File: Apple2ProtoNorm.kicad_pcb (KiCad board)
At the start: 2 copper layers, 177.8 x 76.4 mm, 3 parts, among them J1 Apple II Bus Card Edge, J2 Apple II Bus Card Pin Header

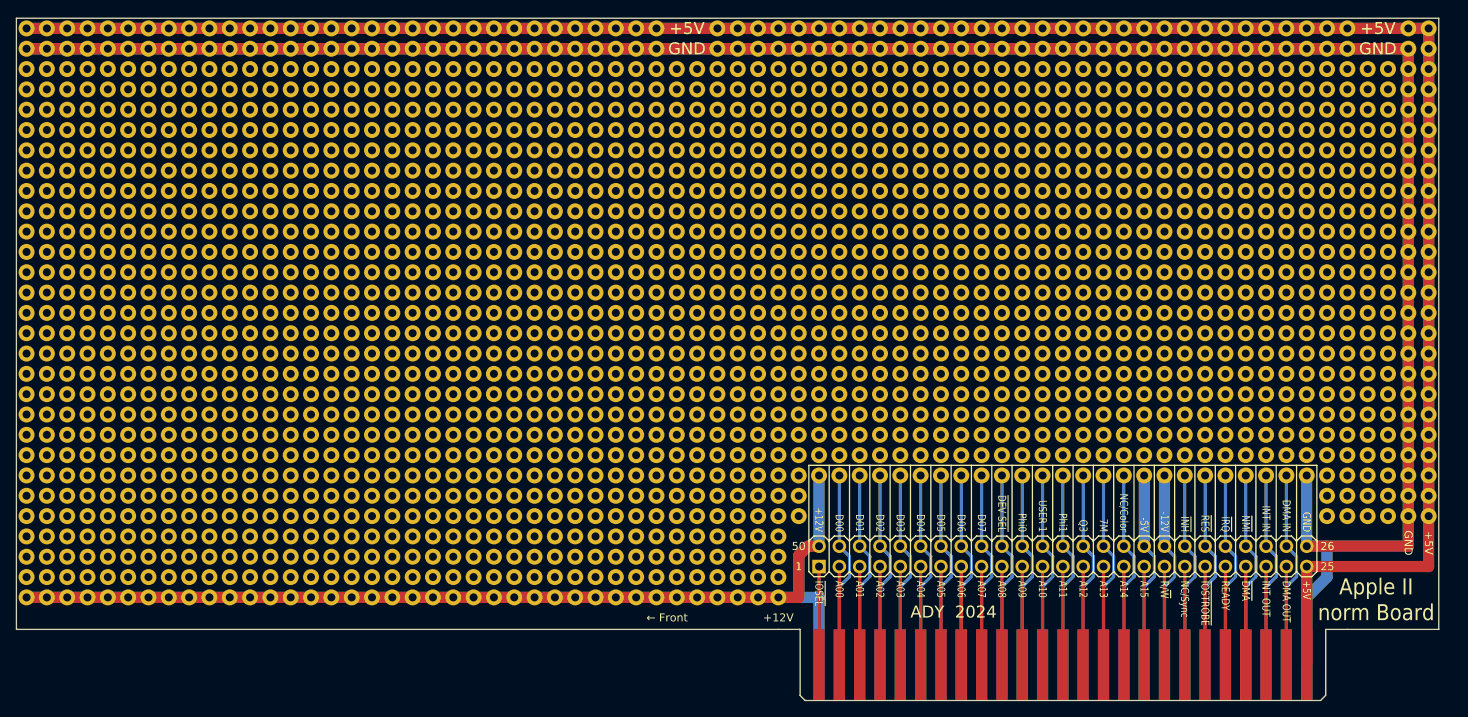
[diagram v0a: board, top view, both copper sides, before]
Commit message: Updated Silk Screen to be easier to read. Added more Apple II documentation.
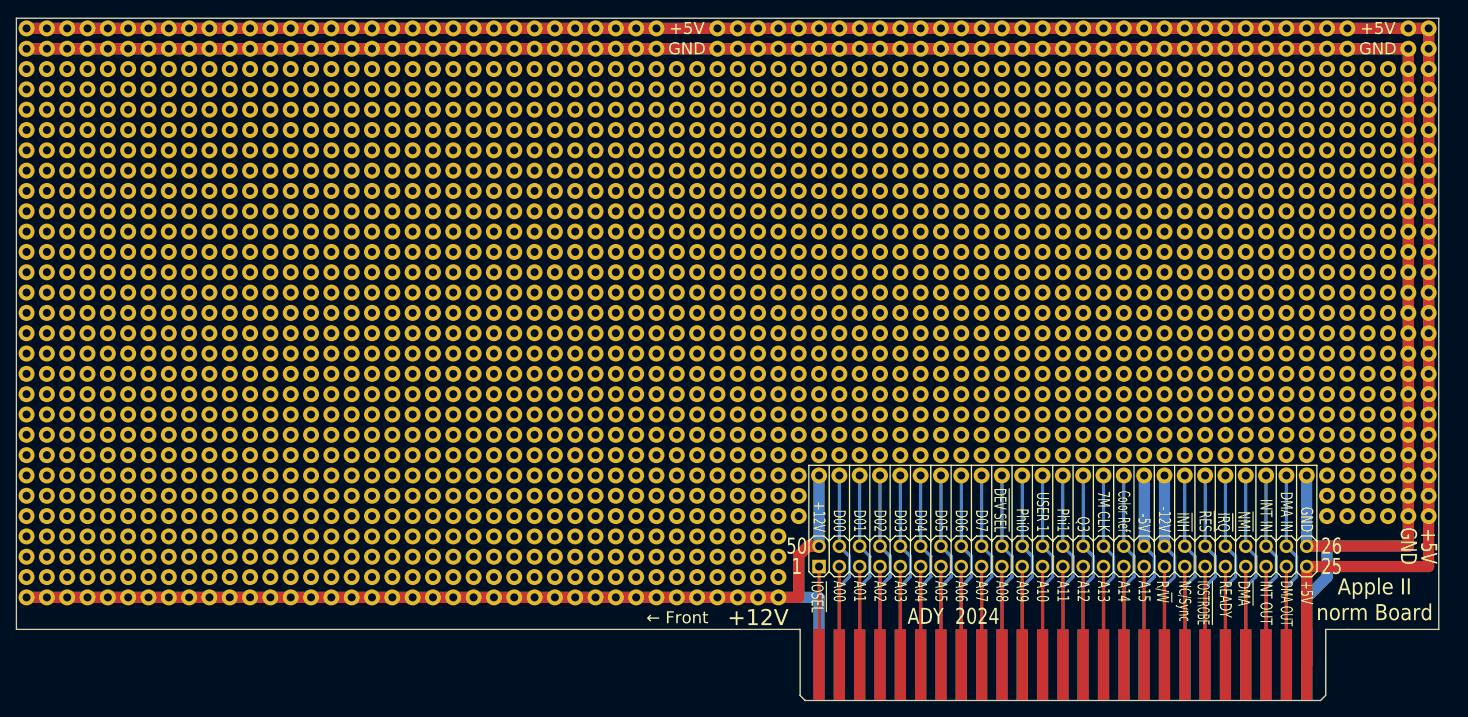
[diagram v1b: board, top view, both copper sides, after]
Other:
- board text added: "7M CLK"
- board text added: "Color Ref"
- board text removed: "7M"
- board text removed: "NC/Color"
